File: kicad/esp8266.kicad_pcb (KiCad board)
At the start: 2 copper layers, 85 x 75 mm, 62 parts, among them J1 BATT, J10 Green, J11 Blue, J12 White, J13 IO_RGBW, J14 +12V, J15 hole, J16 hole, J17 hole, J18 hole, J2 5 / 12V, J3 CONN FT232RL, J4 RJ12-I2C, J5 RJ12-I2C, J6 Onewire, J7 Onewire, J8 Red, J9 Pad, Q1 BSP75, Q2 BSP75, Q3 BSP75, Q4 BSP75, SW1 RESET, SW2 PROG, U1 ESP-12E, U2 MCP73831-2, U3 MCP1703-33, U4 MS5637, U5 MCP1703-50, U6 Si7020-A20, U7 DS18B20

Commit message: final version of V100
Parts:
- removed G***: LOGO, libs:hackuarium
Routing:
- net GND: track 91.0 -> 93.4 mm
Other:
- outline, holes or cut-outs redrawn
- board text added: "12V"
- board text added: "3.3V"
- board text added: "4V"
- board text added: "5V"
- board text added: "BATT"
- board text added: "GND"
- board text added: "IO12"
- board text added: "IO13"
- board text added: "IO14"
- board text added: "IO15"
- board text added: "OW"
- board text added: "PROG"
- board text added: "RESET"
- board text added: "RX"
- board text added: "SCL"
- board text added: "SDA"
- board text added: "TX"

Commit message: move 3d models to shared library
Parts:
- U4: footprint libs:MS5637 -> hackuarium:MS5637
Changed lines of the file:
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@@
       (rotate (xyz 0 0 0))
     )
-    (model ${KIPRJMOD}/3d/esp-12e/ESP8266-12E.stp
+    (model ${HACKUARIUM}/3d/esp-12e/ESP8266-12E.stp
       (offset (xyz 11.5 -13.5 0))
       (scale (xyz 1 1 1))
@@
       (rotate (xyz 0 0 0))
     )
-    (model ${KIPRJMOD}/3d/ej503a-barrel-power-supply/MPD_EJ503A.step
+    (model ${HACKUARIUM}/3d/ej503a-barrel-power-supply/MPD_EJ503A.step
       (offset (xyz -14 0 0))
       (scale (xyz 1 1 1))
@@
       (net 1 GND))
     (pad "" np_thru_hole circle (at 8.25 8.89 270) (size 3.25 3.25) (drill 3.25) (layers *.Cu *.Mask))
-    (model ${KISYS3DMOD}/Connector_RJ.3dshapes/RJ12_Amphenol_54601.wrl
-      (at (xyz 0 0 0))
-      (scale (xyz 1 1 1))
-      (rotate (xyz 0 0 0))
-    )
-    (model "${KIPRJMOD}/3d/rj12-connectors-6p6c/rj_6p_615006144121 (rev1).stp"
+    (model "${HACKUARIUM}/3d/rj12-connectors-6p6c/rj_6p_615006144121 (rev1).stp"
       (offset (xyz 3 -7.5 8))
       (scale (xyz 1 1 1))
@@
       (net 1 GND))
     (pad "" np_thru_hole circle (at 8.25 8.89 270) (size 3.25 3.25) (drill 3.25) (layers *.Cu *.Mask))
-    (model "${KIPRJMOD}/3d/rj12-connectors-6p6c/rj_6p_615006144121 (rev1).stp"
+    (model "${HACKUARIUM}/3d/rj12-connectors-6p6c/rj_6p_615006144121 (rev1).stp"
       (offset (xyz 3 -8 8))
       (scale (xyz 1 1 1))
@@
       (rotate (xyz 0 0 0))
     )
-    (model ${KIPRJMOD}/3d/pj-307-stereo-connector/pj-307.step
+    (model ${HACKUARIUM}/3d/pj-307-stereo-connector/pj-307.step
       (offset (xyz 7.5 10 0))
       (scale (xyz 1 1 1))
@@
       (rotate (xyz 0 0 0))
     )
-    (model ${KIPRJMOD}/3d/pj-307-stereo-connector/pj-307.step
+    (model ${HACKUARIUM}/3d/pj-307-stereo-connector/pj-307.step
       (offset (xyz 7.5 10 0))
       (scale (xyz 1 1 1))
@@
     )
   )
-  (module libs:MS5637 (layer F.Cu)
+  (module hackuarium:MS5637 (layer F.Cu)
     (at 145.31 122.395)
     (solder_paste_margin -0.08)

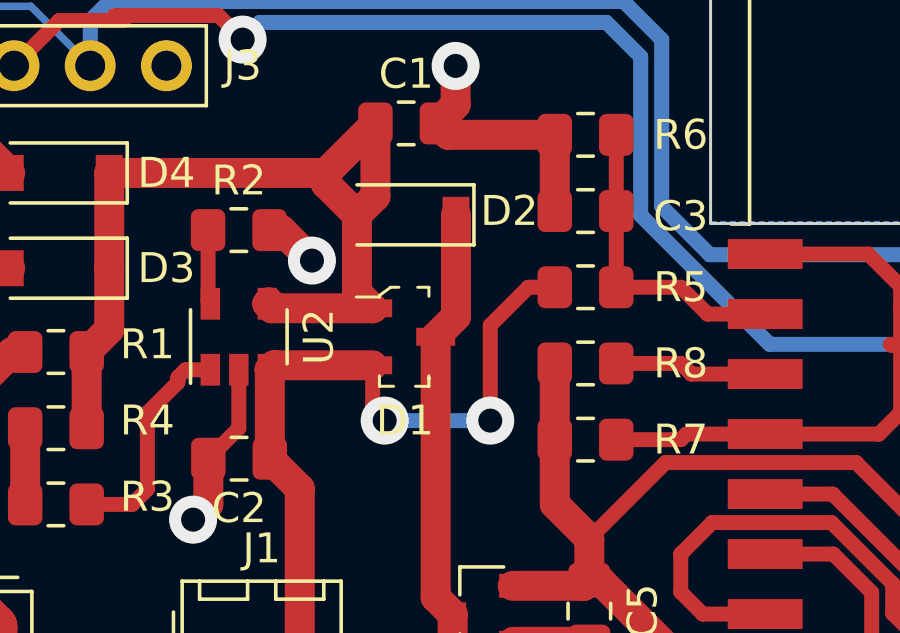
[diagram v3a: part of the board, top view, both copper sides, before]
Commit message: move sub schemas
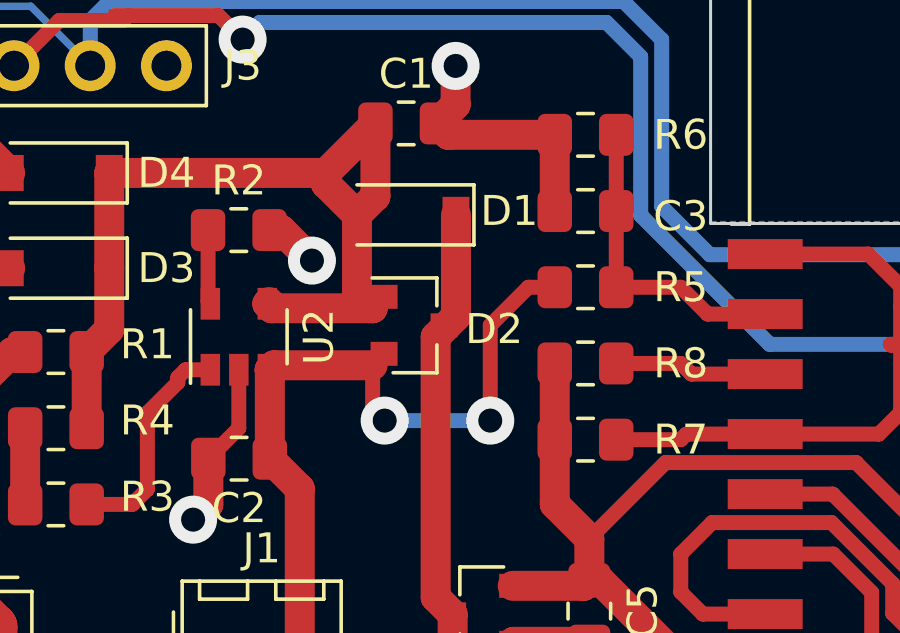
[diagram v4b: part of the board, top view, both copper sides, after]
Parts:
- removed the D1 at (108.2, 73.9)
- added D2: DMP1045U, Package_TO_SOT_SMD:SOT-23, F.Cu at (108.5, 73.5)
- renumbered D2 to D1
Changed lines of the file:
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@@
     (add_net "Net-(U6-Pad7)")
+  )
+  (module Package_TO_SOT_SMD:SOT-23 (layer F.Cu)
+    (at 108.48 73.5)
+    (descr "SOT-23, Standard")
+    (tags SOT-23)
+    (attr smd)
+    (fp_text reference D2 (at 2.667 0.127) (layer F.SilkS)
+      (effects (font (size 1 1) (thickness 0.15)))
+    )
+    (fp_text value DMP1045U (at 0 2.5) (layer F.Fab)
+      (effects (font (size 1 1) (thickness 0.15)))
+    )
+    (fp_text user %R (at 0 0 90) (layer F.Fab)
+      (effects (font (size 0.5 0.5) (thickness 0.075)))
+    )
+    (fp_line (start -0.7 -0.95) (end -0.7 1.5) (layer F.Fab) (width 0.1))
+    (fp_line (start -0.15 -1.52) (end 0.7 -1.52) (layer F.Fab) (width 0.1))
+    (fp_line (start -0.7 -0.95) (end -0.15 -1.52) (layer F.Fab) (width 0.1))
+    (fp_line (start 0.7 -1.52) (end 0.7 1.52) (layer F.Fab) (width 0.1))
+    (fp_line (start -0.7 1.52) (end 0.7 1.52) (layer F.Fab) (width 0.1))
+    (fp_line (start 0.76 1.58) (end 0.76 0.65) (layer F.SilkS) (width 0.12))
+    (fp_line (start 0.76 -1.58) (end 0.76 -0.65) (layer F.SilkS) (width 0.12))
+    (fp_line (start -1.7 -1.75) (end 1.7 -1.75) (layer F.CrtYd) (width 0.05))
+    (fp_line (start 1.7 -1.75) (end 1.7 1.75) (layer F.CrtYd) (width 0.05))
+    (fp_line (start 1.7 1.75) (end -1.7 1.75) (layer F.CrtYd) (width 0.05))
+    (fp_line (start -1.7 1.75) (end -1.7 -1.75) (layer F.CrtYd) (width 0.05))
+    (fp_line (start 0.76 -1.58) (end -1.4 -1.58) (layer F.SilkS) (width 0.12))
+    (fp_line (start 0.76 1.58) (end -0.7 1.58) (layer F.SilkS) (width 0.12))
+    (pad 1 smd rect (at -1 -0.95) (size 0.9 0.8) (layers F.Cu F.Paste F.Mask)
+      (net 2 /MCP73831/VIN))
+    (pad 2 smd rect (at -1 0.95) (size 0.9 0.8) (layers F.Cu F.Paste F.Mask)
+      (net 42 +BATT))
+    (pad 3 smd rect (at 1 0) (size 0.9 0.8) (layers F.Cu F.Paste F.Mask)
+      (net 20 /MCP1703-33/VDD))
+    (model ${KISYS3DMOD}/Package_TO_SOT_SMD.3dshapes/SOT-23.wrl
+      (at (xyz 0 0 0))
+      (scale (xyz 1 1 1))
+      (rotate (xyz 0 0 0))
+    )
   )
   (module MountingHole:MountingHole_3.2mm_M3 (layer F.Cu)
@@
     )
   )
-  (module digikey-footprints:SOT-23-3 (layer F.Cu)
-    (at 108.15 73.881)
-    (fp_text reference D1 (at 0.025 2.794) (layer F.SilkS)
-      (effects (font (size 1 1) (thickness 0.15)))
-    )
-    (fp_text value DMP1045U (at 0.025 3.25) (layer F.Fab)
-      (effects (font (size 1 1) (thickness 0.15)))
-    )
-    (fp_line (start 0.7 1.52) (end 0.7 -1.52) (layer F.Fab) (width 0.1))
-    (fp_line (start -0.7 1.52) (end 0.7 1.52) (layer F.Fab) (width 0.1))
-    (fp_text user %R (at -0.125 0.15) (layer F.Fab)
-      (effects (font (size 0.25 0.25) (thickness 0.05)))
-    )
-    (fp_line (start 0.825 -1.65) (end 0.825 -1.35) (layer F.SilkS) (width 0.1))
-    (fp_line (start 0.45 -1.65) (end 0.825 -1.65) (layer F.SilkS) (width 0.1))
-    (fp_line (start 0.825 1.65) (end 0.375 1.65) (layer F.SilkS) (width 0.1))
-    (fp_line (start 0.825 1.35) (end 0.825 1.65) (layer F.SilkS) (width 0.1))
-    (fp_line (start 0.825 1.425) (end 0.825 1.3) (layer F.SilkS) (width 0.1))
-    (fp_line (start -0.825 1.65) (end -0.825 1.3) (layer F.SilkS) (width 0.1))
-    (fp_line (start -0.35 1.65) (end -0.825 1.65) (layer F.SilkS) (width 0.1))
-    (fp_line (start -0.425 -1.525) (end -0.7 -1.325) (layer F.Fab) (width 0.1))
-    (fp_line (start -0.425 -1.525) (end 0.7 -1.525) (layer F.Fab) (width 0.1))
-    (fp_line (start -0.7 -1.325) (end -0.7 1.525) (layer F.Fab) (width 0.1))
-    (fp_line (start -0.825 -1.325) (end -1.6 -1.325) (layer F.SilkS) (width 0.1))
-    (fp_line (start -0.825 -1.375) (end -0.825 -1.325) (layer F.SilkS) (width 0.1))
-    (fp_line (start -0.45 -1.65) (end -0.825 -1.375) (layer F.SilkS) (width 0.1))
-    (fp_line (start -0.175 -1.65) (end -0.45 -1.65) (layer F.SilkS) (width 0.1))
-    (fp_line (start 1.825 -1.95) (end 1.825 1.95) (layer F.CrtYd) (width 0.05))
-    (fp_line (start 1.825 1.95) (end -1.825 1.95) (layer F.CrtYd) (width 0.05))
-    (fp_line (start -1.825 -1.95) (end -1.825 1.95) (layer F.CrtYd) (width 0.05))
-    (fp_line (start -1.825 -1.95) (end 1.825 -1.95) (layer F.CrtYd) (width 0.05))
-    (pad 1 smd rect (at -1.05 -0.95) (size 1.3 0.6) (layers F.Cu F.Paste F.Mask)
-      (net 2 /MCP73831/VIN) (solder_mask_margin 0.07))
-    (pad 2 smd rect (at -1.05 0.95) (size 1.3 0.6) (layers F.Cu F.Paste F.Mask)
-      (net 42 +BATT) (solder_mask_margin 0.07))
-    (pad 3 smd rect (at 1.05 0) (size 1.3 0.6) (layers F.Cu F.Paste F.Mask)
-      (net 20 /MCP1703-33/VDD) (solder_mask_margin 0.07))
-    (model ${KISYS3DMOD}/Package_TO_SOT_SMD.3dshapes/SOT-23.wrl
-      (at (xyz 0 0 0))
-      (scale (xyz 1 1 1))
-      (rotate (xyz 0 0 0))
-    )
-  )
   (module Diode_SMD:D_SOD-123 (layer F.Cu)
     (at 108.226 69.817 180)
@@
     (tags SOD-123)
     (attr smd)
-    (fp_text reference D2 (at -3.429 0.127 180) (layer F.SilkS)
-      (effects (font (size 1 1) (thickness 0.15)))
-    )
+    (fp_text reference D1 (at -3.429 0.127 180) (layer F.SilkS)
+      (effects (font (size 1 1) (thickness 0.15)))
+    )

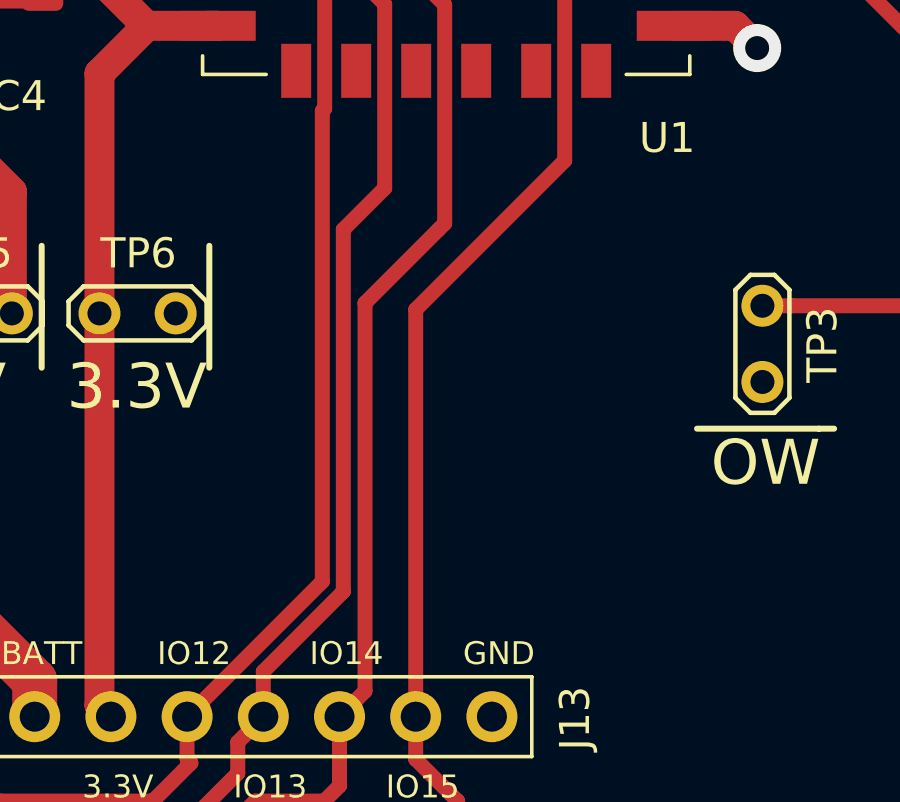
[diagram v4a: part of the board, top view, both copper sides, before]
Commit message: pub back hackuarium logo on pcb
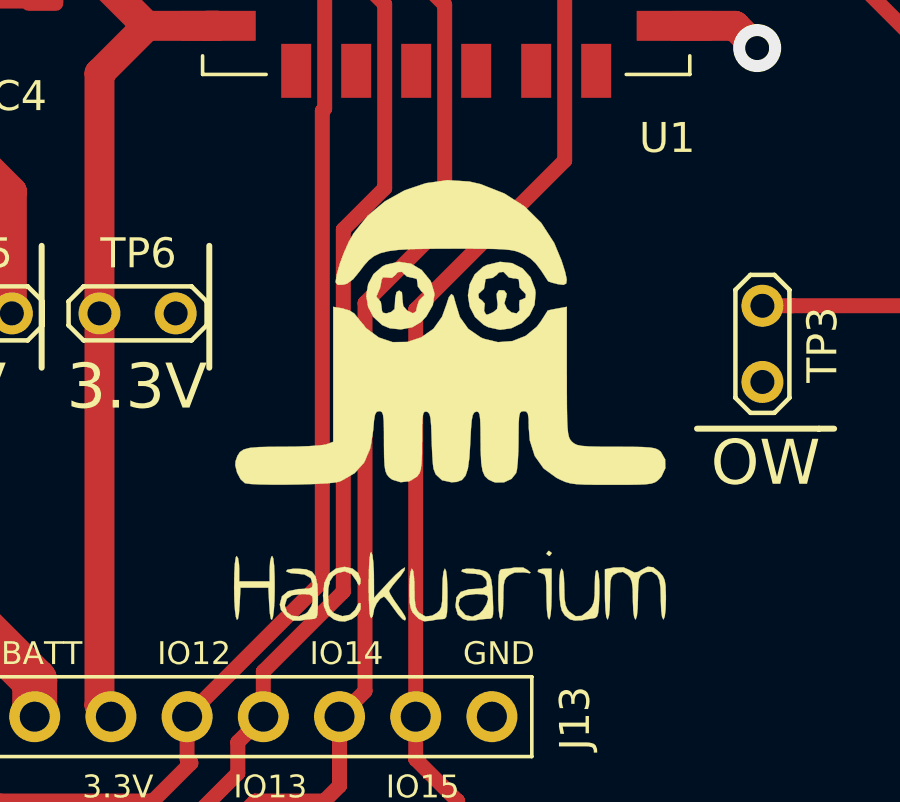
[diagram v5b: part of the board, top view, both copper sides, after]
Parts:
- added G***: LOGO, hackuarium:hackuarium, F.Cu at (127.9, 97.6)
